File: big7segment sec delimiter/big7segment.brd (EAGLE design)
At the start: 20.3 x 121.9 mm, 13 parts, among them Q19 NMOS

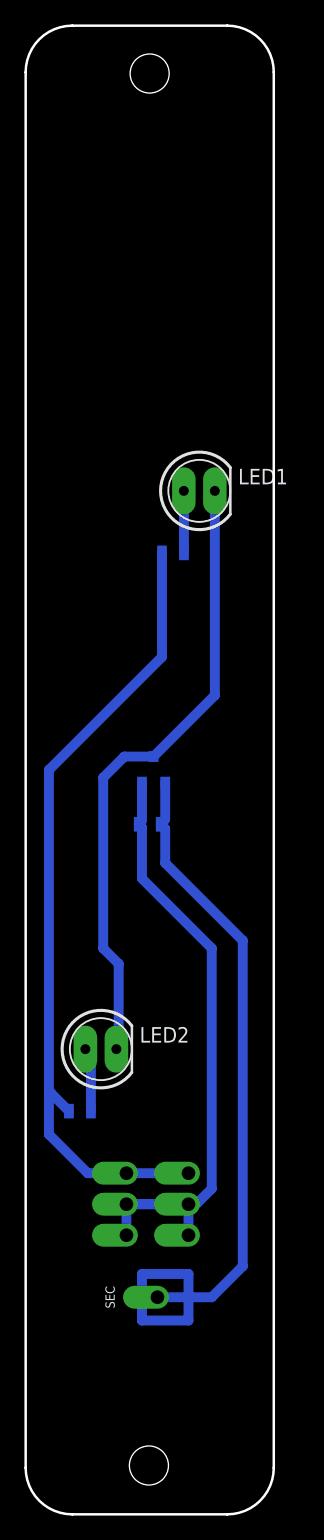
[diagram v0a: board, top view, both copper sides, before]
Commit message: thicker big segment 7 sec
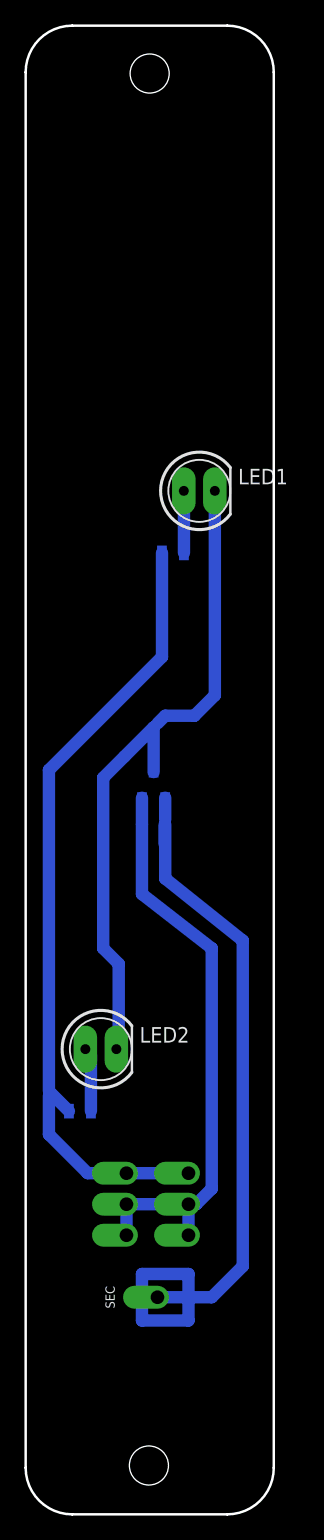
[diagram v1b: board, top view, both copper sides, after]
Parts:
- moved R70 1.63 mm to (10.5, 54.9)
- moved Q19 1.27 mm to (10.5, 59.7)
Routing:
- net N$75: track 51.5 -> 55.2 mm
- net GND_SEC: track 53.5 -> 54.1 mm
